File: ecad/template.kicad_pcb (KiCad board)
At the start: 2 copper layers, 25.2 x 27.3 mm, 3 parts, among them P1 CF_EXP_LEFT, P2 CF_EXP_RIGHT

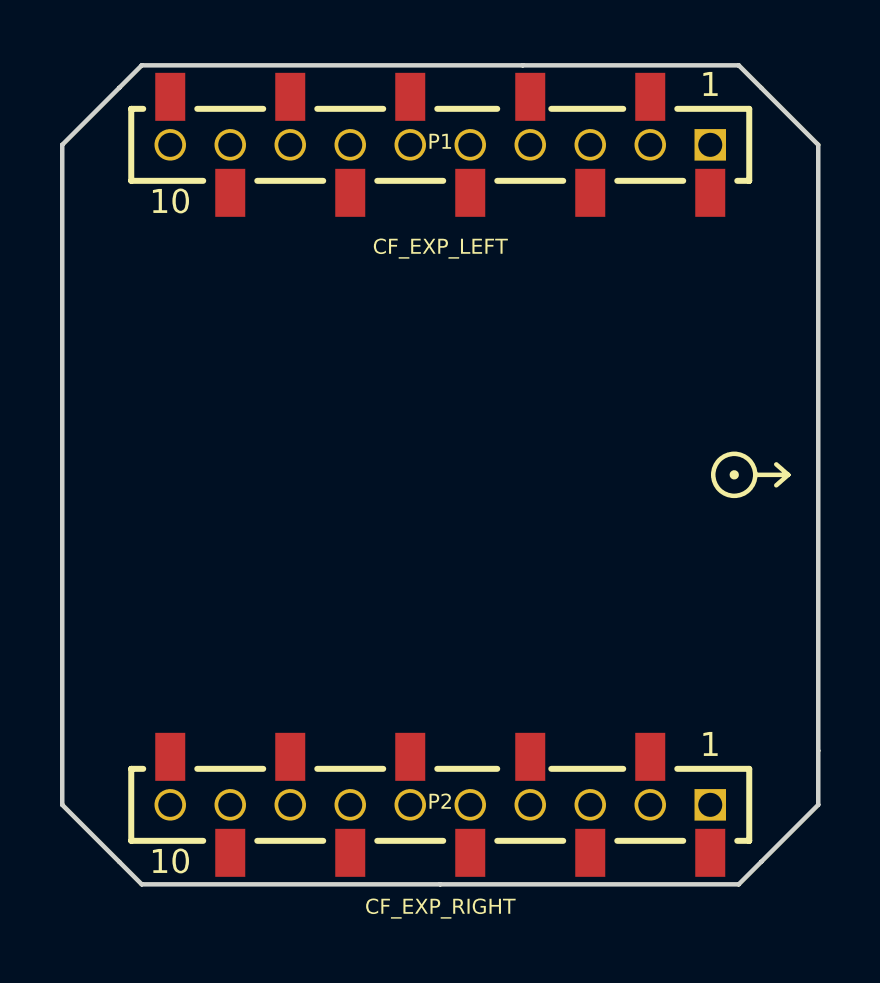
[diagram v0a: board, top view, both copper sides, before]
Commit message: Expansion connector lib added and project updated to use this.
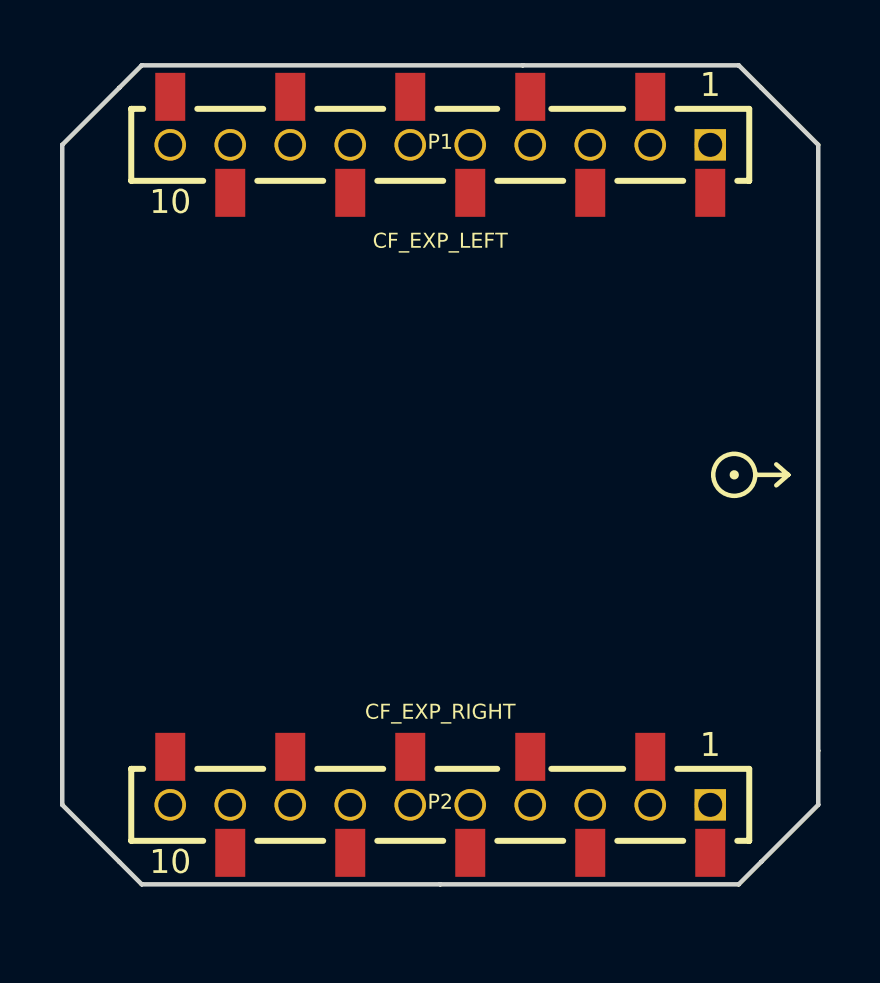
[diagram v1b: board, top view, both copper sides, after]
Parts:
- EXP_ORIENTATION: value VAL** -> ORIENTATION
- P1, P2: footprint connectors:BF090-10-X-B2 -> connectors:CF2-EXP-SMD-HOLES
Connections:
- P1 pad 1: Net-(P1-Pad1) -> (no net)
- P1 pad 10: Net-(P1-Pad10) -> (no net)
- P1 pad 2: Net-(P1-Pad2) -> (no net)
- P1 pad 3: Net-(P1-Pad3) -> (no net)
- P1 pad 4: Net-(P1-Pad4) -> (no net)
- P1 pad 5: Net-(P1-Pad5) -> (no net)
- P1 pad 6: Net-(P1-Pad6) -> (no net)
- P1 pad 7: Net-(P1-Pad7) -> (no net)
- P1 pad 8: Net-(P1-Pad8) -> (no net)
- P1 pad 9: Net-(P1-Pad9) -> (no net)
- P2 pad 1: Net-(P2-Pad1) -> (no net)
- P2 pad 10: Net-(P2-Pad10) -> (no net)
- P2 pad 2: Net-(P2-Pad2) -> (no net)
- P2 pad 3: Net-(P2-Pad3) -> (no net)
- P2 pad 4: Net-(P2-Pad4) -> (no net)
- P2 pad 5: Net-(P2-Pad5) -> (no net)
- P2 pad 6: Net-(P2-Pad6) -> (no net)
- P2 pad 7: Net-(P2-Pad7) -> (no net)
- P2 pad 8: Net-(P2-Pad8) -> (no net)
- P2 pad 9: Net-(P2-Pad9) -> (no net)

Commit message: Updated to new CF2 deck footprint which works better for SMT production.
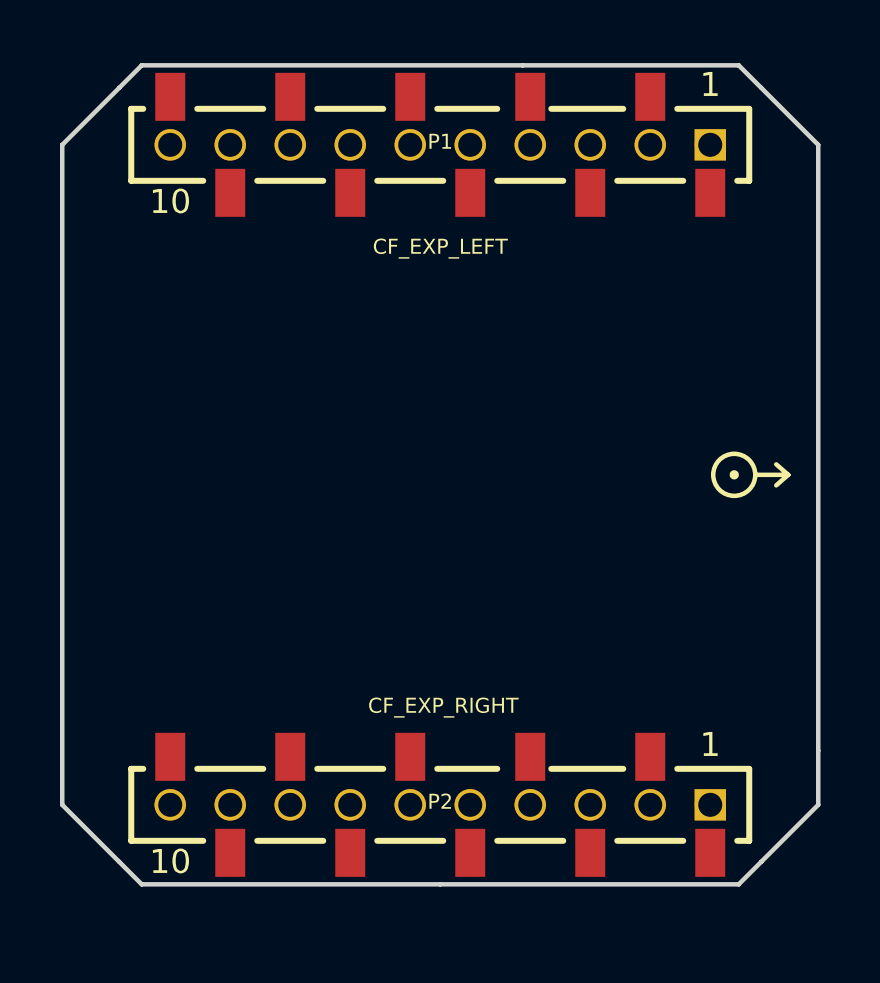
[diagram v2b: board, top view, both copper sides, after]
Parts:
- EXP_ORIENTATION: value ORIENTATION -> VAL**
- P1, P2: footprint connectors:CF2-EXP-SMD-HOLES -> connectors:BF090-10-X-B2
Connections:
- P1 pad 1: (no net) -> Net-(P1-Pad1)
- P1 pad 10: (no net) -> Net-(P1-Pad10)
- P1 pad 2: (no net) -> Net-(P1-Pad2)
- P1 pad 3: (no net) -> Net-(P1-Pad3)
- P1 pad 4: (no net) -> Net-(P1-Pad4)
- P1 pad 5: (no net) -> Net-(P1-Pad5)
- P1 pad 6: (no net) -> Net-(P1-Pad6)
- P1 pad 7: (no net) -> Net-(P1-Pad7)
- P1 pad 8: (no net) -> Net-(P1-Pad8)
- P1 pad 9: (no net) -> Net-(P1-Pad9)
- P2 pad 1: (no net) -> Net-(P2-Pad1)
- P2 pad 10: (no net) -> Net-(P2-Pad10)
- P2 pad 2: (no net) -> Net-(P2-Pad2)
- P2 pad 3: (no net) -> Net-(P2-Pad3)
- P2 pad 4: (no net) -> Net-(P2-Pad4)
- P2 pad 5: (no net) -> Net-(P2-Pad5)
- P2 pad 6: (no net) -> Net-(P2-Pad6)
- P2 pad 7: (no net) -> Net-(P2-Pad7)
- P2 pad 8: (no net) -> Net-(P2-Pad8)
- P2 pad 9: (no net) -> Net-(P2-Pad9)
